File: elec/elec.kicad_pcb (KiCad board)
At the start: 4 copper layers, 58 x 58 mm, 148 parts, among them J1 USB_C_Receptacle, J2 Conn_01x05, J3 Screw_Terminal_01x02, J4 Conn_01x03, J5 Conn_01x03, Q1 AO4419, SW2 SW_Push, SW3 SW_Push, SW4 SW_Push, SW5 SW_Push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

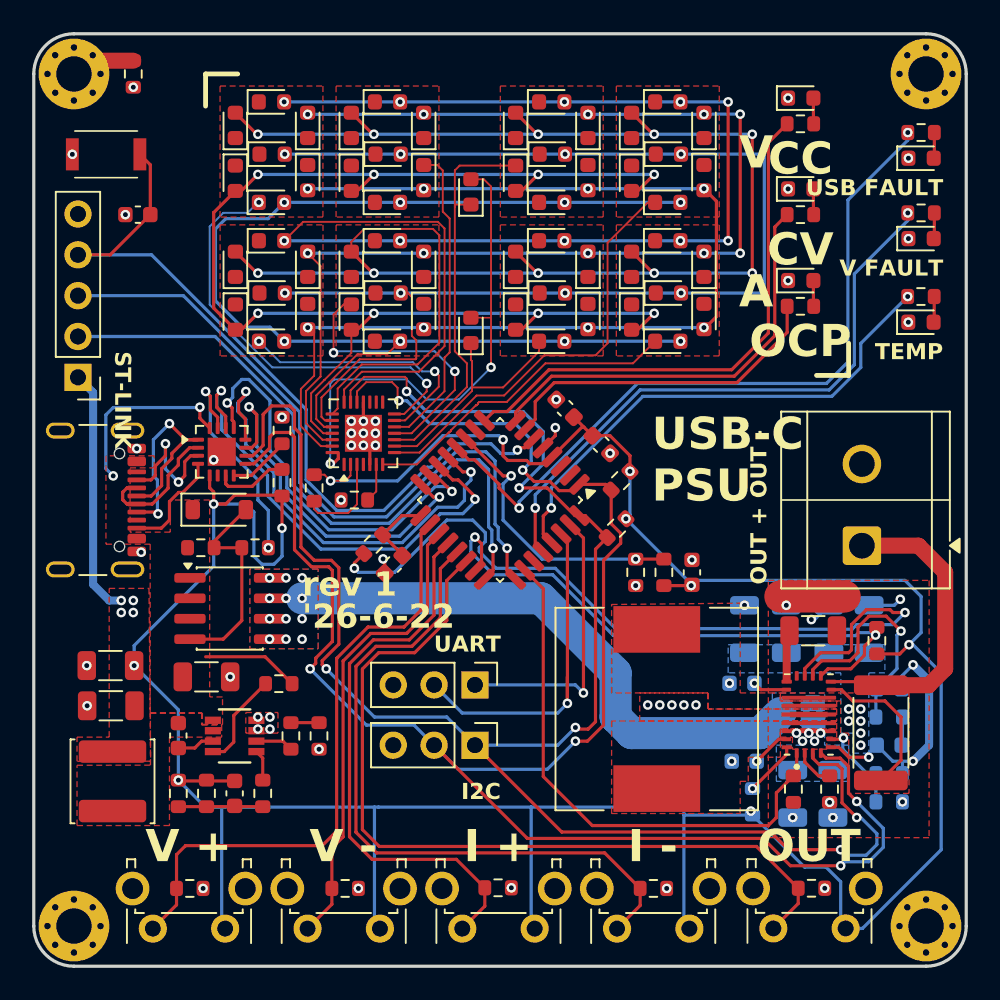
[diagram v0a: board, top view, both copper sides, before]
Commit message: Added Bleed Resistor, Added Buzzer
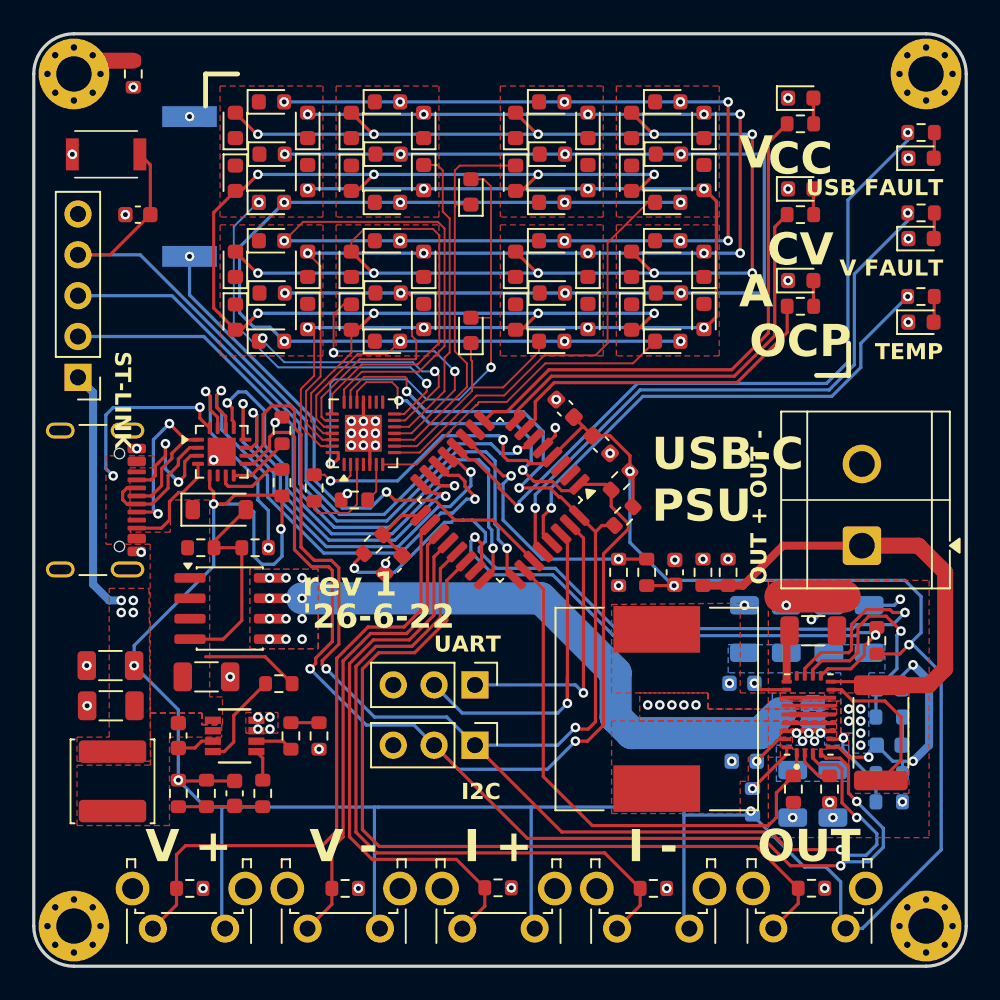
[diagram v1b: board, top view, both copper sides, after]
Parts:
- added BZ1: Buzzer, Buzzer_Beeper:Buzzer_Murata_PKMCS0909E, B.Cu at (104.7, 89.3)
- added R37: 20k, Resistor_SMD:R_0603_1608Metric, F.Cu at (136.6, 113.3)
- added R38: 20k, Resistor_SMD:R_0603_1608Metric, F.Cu at (138.2, 113.3)
- moved C20 1.06 mm to (134.8, 113.3)
- moved R31 1.06 mm to (133.1, 113.3)
- moved TH1 1.06 mm to (131.3, 113.3)
- moved R12 0.87 mm to (131.7, 109.8)
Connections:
- U3 pad 27: unconnected-(U3-PB3-Pad27) -> /BUZZER
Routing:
- net /BUZZER: track 0.00 -> 33.7 mm, vias 0 -> 2
- net VOUT: track 19.5 -> 30.4 mm
- net /display/SEG_D: track 73.4 -> 70.2 mm
- net +3V3: track 215.6 -> 218.4 mm, vias 15 -> 14
- net /display/DIG_7: track 27.2 -> 24.8 mm
- net /USB-C_EN: track 28.8 -> 26.6 mm
- net /USB-C_Fault: track 26.1 -> 24.9 mm
- net GNDREF: track 9.41 -> 10.5 mm, vias 54 -> 57
- net /TEMP_ADC: track 17.7 -> 16.6 mm
- net /SCL: track 117.2 -> 117.7 mm

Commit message: Generate Production files
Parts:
- added R39: 20k, Resistor_SMD:R_0603_1608Metric, F.Cu at (133.2, 113.3)
- R31: value 10k -> 20k
- R7, R8: value 900k -> 1M
- moved R31 1.69 mm to (131.4, 113.3)
- moved TH1 1.69 mm to (129.7, 113.3)
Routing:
- net +3V3: track 218.4 -> 221.8 mm, vias 14 -> 16
- net /SCL: track 117.7 -> 120.7 mm
- net /UART_RX: track 17.8 -> 18.6 mm
- net /SDA: track 120.0 -> 120.8 mm
- net /UART_TX: track 21.6 -> 20.8 mm
- net /TEMP_ADC: vias 2 -> 4

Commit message: Finalise PCB
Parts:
- added C22: 1uF, Capacitor_SMD:C_0603_1608Metric, F.Cu at (103.9, 102.1)
- added C23: 1uF, Capacitor_SMD:C_0603_1608Metric, F.Cu at (112.4, 107.8)
- added C24: 0.1uF, Capacitor_SMD:C_0603_1608Metric, F.Cu at (114.9, 108.3)
- added R40: 1M, Resistor_SMD:R_0603_1608Metric, F.Cu at (112.0, 111.8)
- added R41: 20k, Resistor_SMD:R_0603_1608Metric, F.Cu at (109.7, 101.7)
- moved R30 3.05 mm to (114.9, 109.8), turned to 0 degrees
- moved R29 2.85 mm to (117.2, 110.6), turned to 90 degrees
- moved C21 1.75 mm to (117.2, 114.6)
- moved R32 1.75 mm to (115.9, 113.3)
- moved D1 0.40 mm to (106.5, 109.8)
- moved R6 0.05 mm to (109.2, 127.1)
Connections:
- C5 pad 2: Net-(C5-Pad2) -> Net-(U2-FB)
- R4 pad 2: Net-(C5-Pad2) -> Net-(U2-FB)
- R5 pad 2: Net-(C5-Pad2) -> Net-(U2-FB)
- R6 pad 1: Net-(C5-Pad2) -> Net-(U2-FB)
- R6 pad 2: Net-(U2-FB) -> GNDREF
- U1 pad 6: unconnected-(U1-~{DEBUG}-Pad6) -> Net-(U1-~{DEBUG})
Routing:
- net +3V3: track 221.8 -> 232.5 mm, vias 16 -> 17
- net Net-(U2-FB): track 1.94 -> 10.9 mm
- net Net-(U1-~{DEBUG}): track 0.00 -> 7.70 mm
- net Net-(C5-Pad2): track 5.25 -> 0.00 mm
- net GNDREF: track 10.5 -> 13.8 mm, vias 57 -> 62
- net /USB-C_INT: track 23.0 -> 25.6 mm
- net Net-(U6-~{SDB}): track 5.96 -> 3.81 mm
- net /PB2: track 4.60 -> 6.52 mm
- net /BUCK-BOOST_Current: track 50.6 -> 49.1 mm
- net Net-(U6-R_EXT): track 2.44 -> 3.51 mm
- net /SCL: track 120.7 -> 120.2 mm
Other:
- board text added: "'26-6-25"
- board text added: "USB-C"
- board text removed: "'26-6-22"
- board text removed: "USB-C PSU"
